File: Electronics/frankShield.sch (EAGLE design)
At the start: 9 parts, among them IC1 BD6230F, IC2 BD6230F

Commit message: 1st hack at the shield design for WiFi Frank...
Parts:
- added C1: 1uF, rcl:C-EUC0805
- added IC3: TS5A23157, reprapltd:TS5A23157
- added JP6: (no value), pinhead:PINHD-1X2
- added R1, R3: 15K, rcl:R-EU_M0805
- added R2: 10K, rcl:R-EU_M0805
- added S1: TL36PO, switch:TL36PO
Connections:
- new net N$11: IC3.COM1, U$1.A0
- new net N$12: C1.1, IC3.NO1, R1.1, R2.2
- new net N$13: JP1.2, S1.P
- new net N$14: IC3.NC1, JP6.1, R3.1
- new net N$15: IC3.IN1, U$1.D2
- net +3V3: now also IC3.+VDD, R3.2
- net GND: now also C1.2, IC3.GND, JP6.2, R2.1, U$1.GND2
- net N$7: now also U$1.D6; no longer U$1.D5
- net N$8: now also U$1.D5; no longer U$1.D6
- net V+: now also R1.2, S1.S; no longer JP1.2
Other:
- note added: "C"
- note added: "E"
- note added: "Frank The Robot EPS8266/Arduino Shield V1.0 reprapltd.com Licence: GPL"
- note added: "LIDAR"
- note added: "Left Motor"
- note added: "Power In"
- note added: "Power To Arduino"
- note added: "Right Motor"
- note added: "phototransistor"
- moved on the sheet: JP1

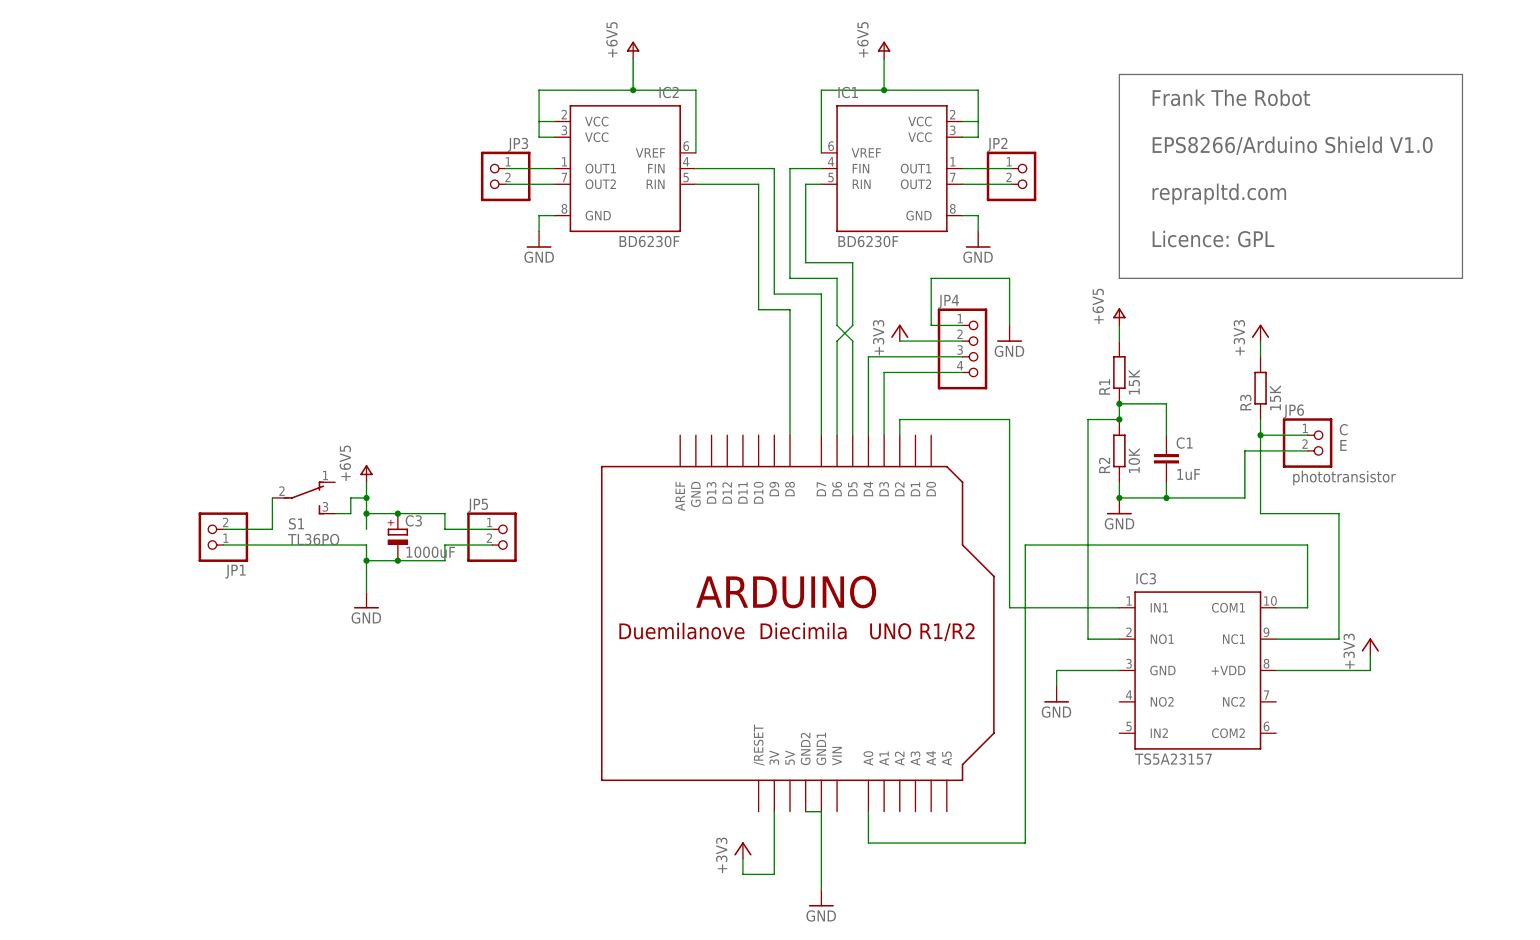
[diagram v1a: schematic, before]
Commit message: Improved shield design. GERBER files added.
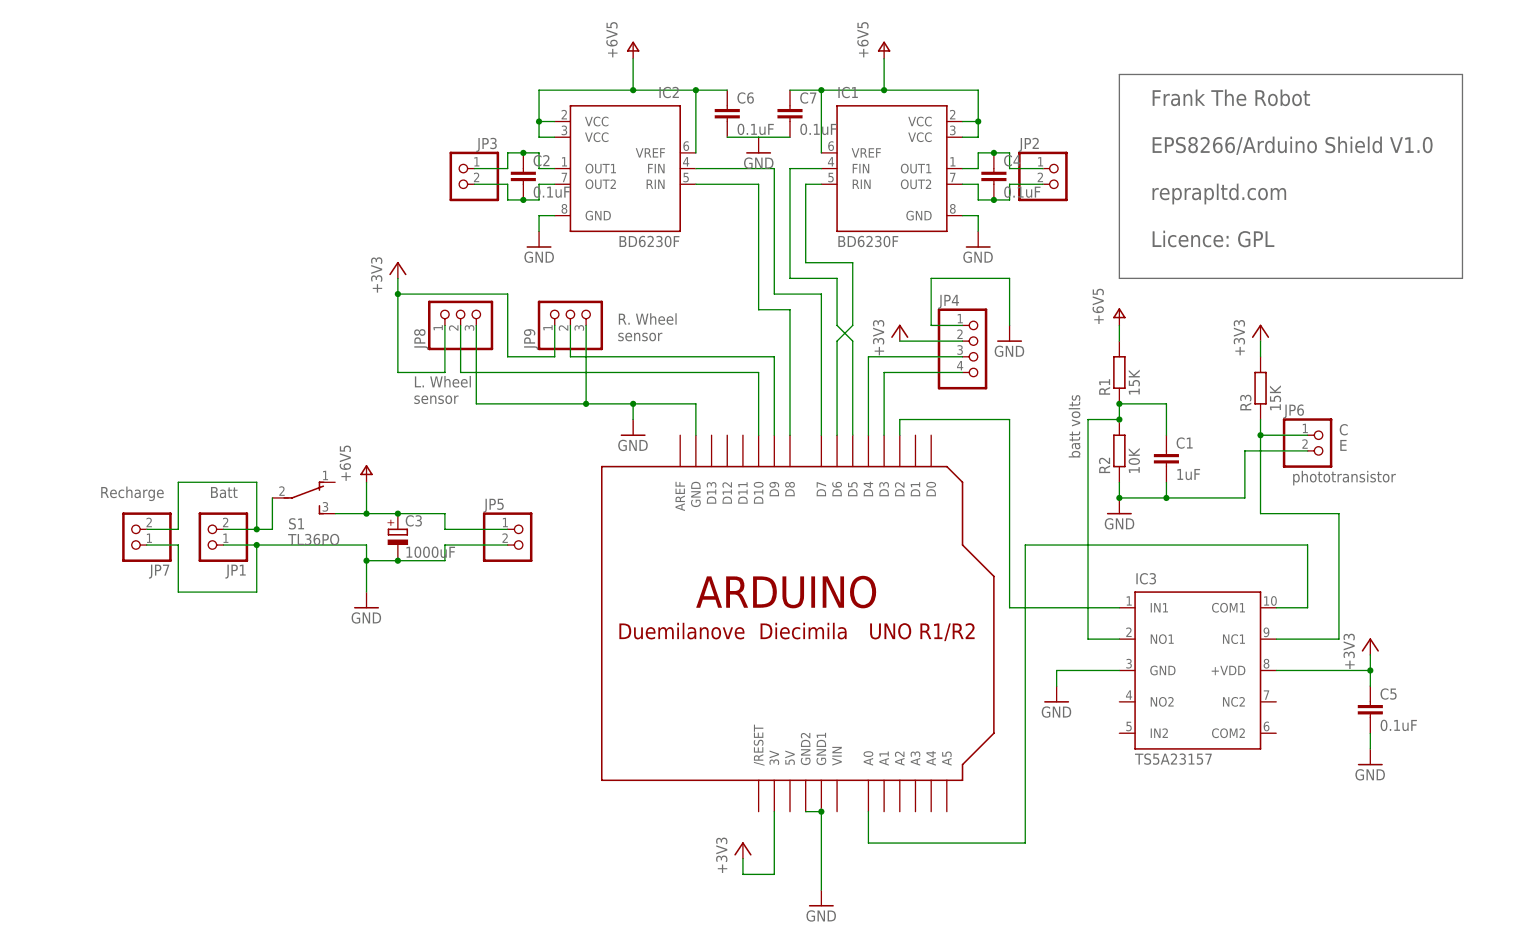
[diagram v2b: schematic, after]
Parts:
- added C2, C4, C5, C6, C7: 0.1uF, rcl:C-EUC0805
- added JP7: (no value), pinhead:PINHD-1X2
- added JP8, JP9: (no value), pinhead:PINHD-1X3
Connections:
- new net N$17: JP9.2, U$1.D9
- new net N$18: JP8.2, U$1.D10
- net +3V3: now also C5.1, JP8.1, JP9.1
- net GND: now also C5.2, C6.2, C7.2, JP7.1, JP8.3, JP9.3, U$1.GND
- net N$13: now also JP7.2
- net N$3: now also C2.1, IC2.OUT1, JP3.1; no longer IC1.OUT1, JP2.1
- net N$4: now also C2.2, IC2.OUT2, JP3.2; no longer IC1.OUT2, JP2.2
- net N$5: now also C4.1, IC1.OUT1, JP2.1; no longer IC2.OUT1, JP3.1
- net N$6: now also C4.2, IC1.OUT2, JP2.2; no longer IC2.OUT2, JP3.2
- net V+: now also C6.1, C7.1
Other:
- note added: "Batt"
- note added: "L. Wheel sensor"
- note added: "R. Wheel sensor"
- note added: "Recharge"
- note added: "batt volts"
- moved on the sheet: JP2, JP3, JP5

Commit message: Updated electronics to power the wheel sensors directly off the battery. (They take too much current from 3V3 if that is used; the sensors now have potential dividers so their output never exceeds 3v3.)
Added a PCB test program for the Wemos D1/ESP8266 board (W.I.P.)
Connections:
- net +3V3: no longer JP8.1, JP9.1
- net V+: now also JP8.1, JP9.1
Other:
- note added: "Note: wheel sensors take too much current to run off 3v3."
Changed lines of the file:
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@@
 <part name="JP8" library="pinhead" deviceset="PINHD-1X3" device=""/>
 <part name="JP9" library="pinhead" deviceset="PINHD-1X3" device=""/>
-<part name="+3V5" library="supply1" deviceset="+3V3" device=""/>
 <part name="C2" library="rcl" deviceset="C-EU" device="C0805" value="0.1uF"/>
 <part name="C4" library="rcl" deviceset="C-EU" device="C0805" value="0.1uF"/>
@@
 <part name="C7" library="rcl" deviceset="C-EU" device="C0805" value="0.1uF"/>
 <part name="GND10" library="supply1" deviceset="GND" device=""/>
+<part name="P+5" library="supply1" deviceset="V+" device="" value="+6V5"/>
 </parts>
 <sheets>
@@
 sensor</text>
 <text x="90.17" y="74.93" size="1.778" layer="96" rot="R90">batt volts</text>
+<text x="-78.74" y="114.3" size="1.778" layer="95">Note: wheel sensors take too much current to run off 3v3.</text>
 </plain>
 <instances>
@@
 <instance part="JP8" gate="A" x="-10.16" y="99.06" rot="R90"/>
 <instance part="JP9" gate="A" x="7.62" y="99.06" rot="R90"/>
-<instance part="+3V5" gate="G$1" x="-20.32" y="106.68"/>
 <instance part="C2" gate="G$1" x="0" y="121.92"/>
 <instance part="C4" gate="G$1" x="76.2" y="121.92"/>
@@
 <instance part="C7" gate="G$1" x="43.18" y="132.08"/>
 <instance part="GND10" gate="1" x="38.1" y="124.46" rot="MR0"/>
+<instance part="P+5" gate="1" x="-20.32" y="109.22"/>
 </instances>
 <busses>
@@
 <wire x1="119.38" y1="91.44" x2="119.38" y2="93.98" width="0.1524" layer="91"/>
 </segment>
-<segment>
-<pinref part="JP8" gate="A" pin="1"/>
-<wire x1="-12.7" y1="96.52" x2="-12.7" y2="88.9" width="0.1524" layer="91"/>
-<pinref part="+3V5" gate="G$1" pin="+3V3"/>
-<wire x1="-12.7" y1="88.9" x2="-20.32" y2="88.9" width="0.1524" layer="91"/>
-<wire x1="-20.32" y1="88.9" x2="-20.32" y2="101.6" width="0.1524" layer="91"/>
-<wire x1="-20.32" y1="101.6" x2="-20.32" y2="104.14" width="0.1524" layer="91"/>
-<wire x1="-20.32" y1="101.6" x2="-2.54" y2="101.6" width="0.1524" layer="91"/>
-<wire x1="-2.54" y1="101.6" x2="-2.54" y2="91.44" width="0.1524" layer="91"/>
-<wire x1="-2.54" y1="91.44" x2="5.08" y2="91.44" width="0.1524" layer="91"/>
-<pinref part="JP9" gate="A" pin="1"/>
-<wire x1="5.08" y1="91.44" x2="5.08" y2="96.52" width="0.1524" layer="91"/>
-<junction x="-20.32" y="101.6"/>
-</segment>
 </net>
 <net name="N$1" class="0">
@@
 <wire x1="96.52" y1="96.52" x2="96.52" y2="93.98" width="0.1524" layer="91"/>
 </segment>
-</net>
+<segment>
+<pinref part="JP8" gate="A" pin="1"/>
+<wire x1="-12.7" y1="96.52" x2="-12.7" y2="88.9" width="0.1524" layer="91"/>
+<wire x1="-12.7" y1="88.9" x2="-20.32" y2="88.9" width="0.1524" layer="91"/>
+<wire x1="-20.32" y1="88.9" x2="-20.32" y2="101.6" width="0.1524" layer="91"/>
+<wire x1="-20.32" y1="101.6" x2="-2.54" y2="101.6" width="0.1524" layer="91"/>
+<wire x1="-2.54" y1="101.6" x2="-2.54" y2="91.44" width="0.1524" layer="91"/>
+<wire x1="-2.54" y1="91.44" x2="5.08" y2="91.44" width="0.1524" layer="91"/>
+<pinref part="JP9" gate="A" pin="1"/>
+<wire x1="5.08" y1="91.44" x2="5.08" y2="96.52" width="0.1524" layer="91"/>
+<junction x="-20.32" y="101.6"/>
+<pinref part="P+5" gate="1" pin="V+"/>
+<wire x1="-20.32" y1="101.6" x2="-20.32" y2="106.68" width="0.1524" layer="91"/>
+</segment>
+</net>
